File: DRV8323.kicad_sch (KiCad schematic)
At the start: 32 parts, among them J3 Screw_Terminal_01x02, U10 NTMFS5C628NLT1G, U11 NTMFS5C628NLT1G, U12 NTMFS5C628NLT1G, U13 LM393, U5 DRV8323RSRGZR, U6 NTMFS5C628NLT1G, U7 NTMFS5C628NLT1G, U8 NTMFS5C628NLT1G, U9 NTMFS5C628NLT1G

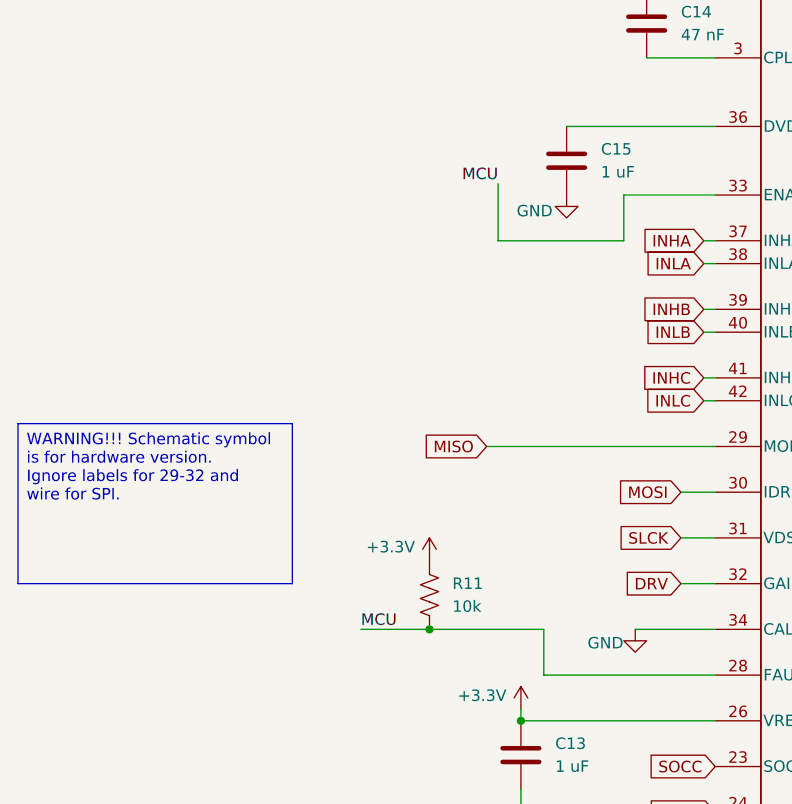
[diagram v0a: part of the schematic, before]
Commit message: Added additional Labels
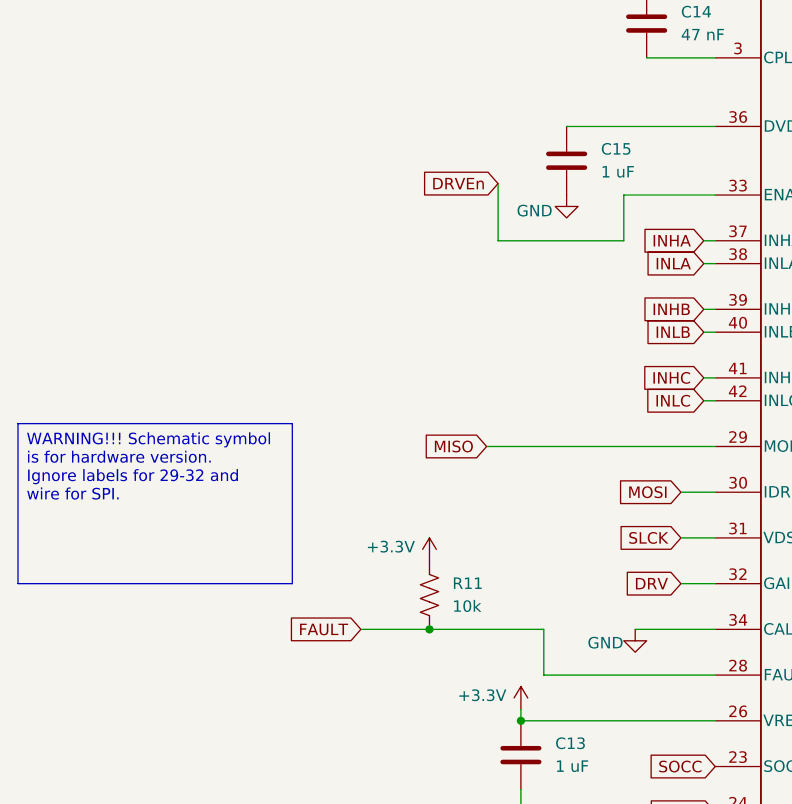
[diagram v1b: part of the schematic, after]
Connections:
- net MCU renamed FAULT
- net FAULT: no longer U5.33 (ENABLE)
- new net DRVEn: U5.33 (ENABLE)
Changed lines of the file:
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@@
-		)
-	)
-	(label "MCU"
-		(at 25.4 110.49 0)
-		(effects
-			(font
-				(size 1.27 1.27)
-			)
-			(justify left bottom)
 		)
 	)
@@
 		)
 	)
-	(label "MCU"
-		(at 40.64 60.96 180)
-		(effects
-			(font
-				(size 1.27 1.27)
-			)
-			(justify right bottom)
-		)
-	)
 	(label "CurrentSense_B"
 		(at 204.47 101.6 180)
@@
 			(effects
 				(font
+					(size 1.27 1.27)
+				)
+				(justify right)
+				(hide yes)
+			)
+		)
+	)
+	(global_label "DRVEn"
+		(shape input)
+		(at 40.64 60.96 180)
+		(fields_autoplaced yes)
+		(effects
+			(font
+				(size 1.27 1.27)
+			)
+			(justify right)
+		)
+		(property "Intersheetrefs" "${INTERSHEET_REFS}"
+			(at 31.7282 60.96 0)
+			(effects
+				(font
+					(size 1.27 1.27)
+				)
+				(justify right)
+				(hide yes)
+			)
+		)
+	)
+	(global_label "FAULT"
+		(shape input)
+		(at 25.4 110.49 180)
+		(fields_autoplaced yes)
+		(effects
+			(font
+				(size 1.27 1.27)
+			)
+			(justify right)
+		)
+		(property "Intersheetrefs" "${INTERSHEET_REFS}"
+			(at 16.9114 110.49 0)
+			(effects
+				(font

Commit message: Layed out PCB
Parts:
- removed C19, C20, C21: 470 uF, symbol Device:C
- added C1, C19, C20: 470 uF, Capacitor_SMD:CP_Elec_10x12.5, symbol Device:C_Polarized
- added J4: Screw_Terminal_01x03, TerminalBlocks:TerminalBlock_MetzConnect_Type703_RT10N03HGLU_1x03_P9.52mm_Horizontal, symbol Connector:Screw_Terminal_01x03
- C13, C15, C16: footprint (none) -> Capacitor_SMD:C_0402_1005Metric
- C14, C17: footprint (none) -> Capacitor_SMD:C_0603_1608Metric
- C18, C22, C23: footprint (none) -> Capacitor_SMD:C_0805_2012Metric
- J3: footprint (none) -> TerminalBlocks:TerminalBlock_MetzConnect_Type703_RT10N02HGLU_1x02_P9.52mm_Horizontal
- NT1: footprint (none) -> NetTie:NetTie-2_SMD_Pad0.5mm
- R11, R12, R13, R14, R15, R16, R17: footprint (none) -> Resistor_SMD:R_0603_1608Metric
- R7, R8, R9: footprint (none) -> Resistor_SMD:R_2512_6332Metric
- U13: footprint (none) -> Package_SO:SOIC-8_3.9x4.9mm_P1.27mm
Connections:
- net +24V: now also C1.1, C19.1, C20.1; no longer J3.1 (Pin_1), U7.5 (DRIAN), U7.6 (EPAD)
- net GND: now also C1.2, C19.2, C20.2
- net PhaseA: now also J4.3 (Pin_3)
- net PhaseB: now also J4.2 (Pin_2)
- net PhaseC: now also U12.1 (SOURCE), U12.2 (SOURCE), U12.3 (SOURCE), U5.19 (SHC), J4.1 (Pin_1)
- new net: J3.1 (Pin_1), U7.5 (DRIAN), U7.6 (EPAD)

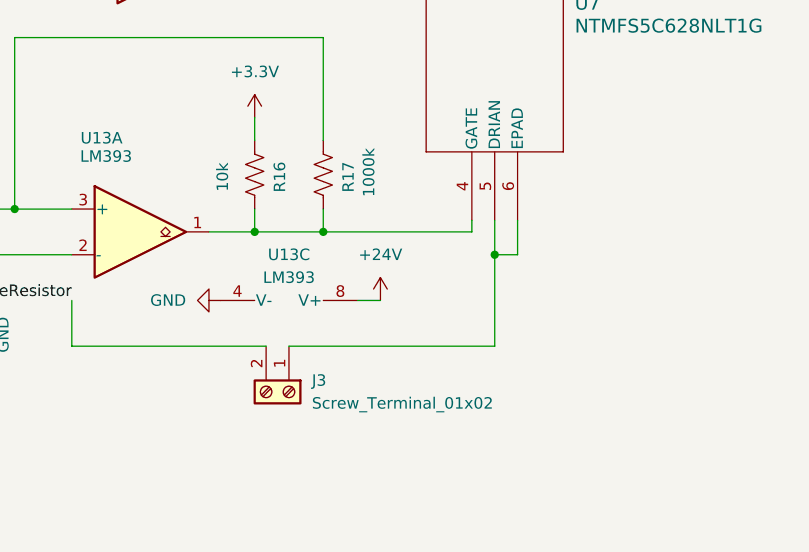
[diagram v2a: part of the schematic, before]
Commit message: finalizing PCB Layouts and traces
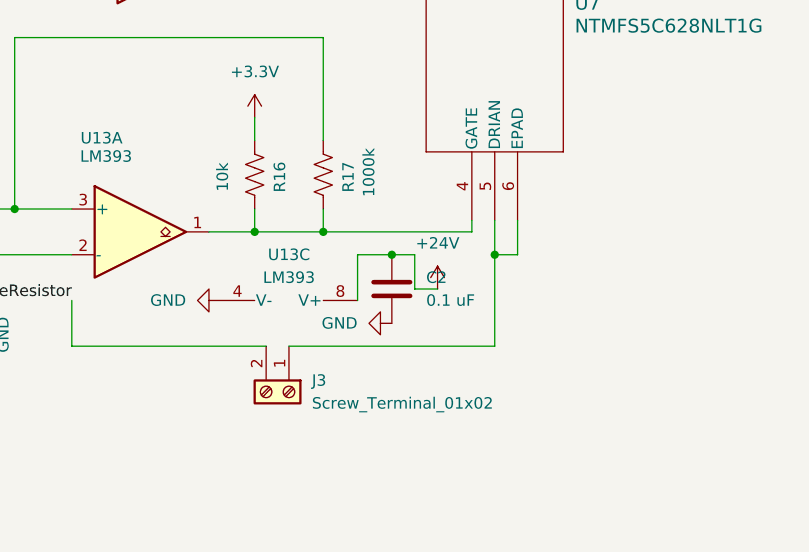
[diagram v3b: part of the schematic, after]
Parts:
- added C2: 0.1 uF, Capacitor_SMD:C_0603_1608Metric, symbol Device:C
- U10, U11, U12, U6, U7, U8, U9: footprint ESP-32-S3-MINI-1:DFN5_5X6_ONS -> ESP-32-S3-MINI-1:NTMF_FET_FIXED
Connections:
- net +24V: now also C2.2
- net GND: now also C2.1
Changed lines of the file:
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@@
 	)
 	(junction
+		(at 257.81 153.67)
+		(diameter 0)
+		(color 0 0 0 0)
+	)
+	(junction
 		(at 215.9 148.59)
 		(diameter 0)
@@
 	(wire
 		(pts
+			(xy 254 158.75) (xy 254 153.67)
+		)
+		(stroke
+			(width 0)
+			(type default)
+		)
+	)
+	(wire
+		(pts
 			(xy 64.77 62.23) (xy 54.61 62.23)
 		)
@@
 	(wire
 		(pts
+			(xy 257.81 153.67) (xy 260.35 153.67)
+		)
+		(stroke
+			(width 0)
+			(type default)
+		)
+	)
+	(wire
+		(pts
 			(xy 201.93 53.34) (xy 201.93 50.8)
 		)
@@
 	(wire
 		(pts
+			(xy 260.35 153.67) (xy 260.35 157.48)
+		)
+		(stroke
+			(width 0)
+			(type default)
+		)
+	)
+	(wire
+		(pts
 			(xy 266.7 104.14) (xy 266.7 101.6)
 		)
@@
 	(wire
 		(pts
+			(xy 260.35 157.48) (xy 262.89 157.48)
+		)
+		(stroke
+			(width 0)
+			(type default)
+		)
+	)
+	(wire
+		(pts
+			(xy 254 153.67) (xy 257.81 153.67)
+		)
+		(stroke
+			(width 0)
+			(type default)
+		)
+	)
+	(wire
+		(pts
 			(xy 48.26 54.61) (xy 64.77 54.61)
 		)
@@
 	(wire
 		(pts
-			(xy 254 158.75) (xy 256.54 158.75)
-		)
-		(stroke
-			(width 0)
-			(type default)
-		)
-	)
-	(wire
-		(pts
 			(xy 110.49 151.13) (xy 115.57 151.13)
 		)
@@
 			)
 		)
-		(property "Footprint" "ESP-32-S3-MINI-1:DFN5_5X6_ONS"
+		(property "Footprint" "ESP-32-S3-MINI-1:NTMF_FET_FIXED"
 			(at 153.67 120.65 0)
 			(effects
@@
 	(symbol
 		(lib_id "Device:C")
+		(at 257.81 157.48 180)
+		(unit 1)
+		(exclude_from_sim no)
+		(in_bom yes)
+		(on_board yes)
+		(dnp no)
+		(fields_autoplaced yes)
+		(property "Reference" "C2"
+			(at 261.62 156.2099 0)
+			(effects
+				(font
+					(size 1.27 1.27)
+				)
+				(justify right)
+			)
+		)
+		(property "Value" "0.1 uF"
+			(at 261.62 158.7499 0)
+			(effects
+				(font
+					(size 1.27 1.27)
+				)
+				(justify right)
+			)
+		)
+		(property "Footprint" "Capacitor_SMD:C_0603_1608Metric"
+			(at 256.8448 153.67 0)
+			(effects
+				(font
+					(size 1.27 1.27)
+				)
+				(hide yes)
+			)
+		)
+		(property "Datasheet" "~"
+			(at 257.81 157.48 0)
+			(effects
+				(font
+					(size 1.27 1.27)
+				)
+				(hide yes)
+			)
+		)
+		(property "Description" "Unpolarized capacitor"
+			(at 257.81 157.48 0)
+			(effects
+				(font
+					(size 1.27 1.27)
+				)
+				(hide yes)
+			)
+		)
+		(pin "2"
+		)
+		(pin "1"
+		)
+		(instances
+			(project "Motor_driver_board"
+				(path "/d384c841-cbb4-43a6-88c3-e1bf606ffd62/b93c4029-f99b-4aa0-b921-a6e9eb4bda3c"
+					(reference "C2")
+					(unit 1)
+				)
+			)
+		)
+	)
+	(symbol
+		(lib_id "Device:C")
 		(at 57.15 43.18 0)
 		(unit 1)
@@
 	(symbol
 		(lib_id "power:+24V")
-		(at 256.54 158.75 0)
+		(at 262.89 157.48 0)
 		(unit 1)
 		(exclude_from_sim no)
@@
 		(fields_autoplaced yes)
 		(property "Reference" "#PWR065"
-			(at 256.54 162.56 0)
+			(at 262.89 161.29 0)
 			(effects
 				(font
@@
 		)
 		(property "Value" "+24V"
-			(at 256.54 153.67 0)
+			(at 262.89 152.4 0)
 			(effects
 				(font
@@
 		)
 		(property "Footprint" ""
-			(at 256.54 158.75 0)
+			(at 262.89 157.48 0)
 			(effects
 				(font
@@
 		)
 		(property "Datasheet" ""
-			(at 256.54 158.75 0)
+			(at 262.89 157.48 0)
 			(effects
 				(font
@@
 		)
 		(property "Description" "Power symbol creates a global label with name \"+24V\""
-			(at 256.54 158.75 0)
+			(at 262.89 157.48 0)
 			(effects
 				(font
@@
 			)
 		)
-		(property "Footprint" "ESP-32-S3-MINI-1:DFN5_5X6_ONS"
+		(property "Footprint" "ESP-32-S3-MINI-1:NTMF_FET_FIXED"
 			(at 271.78 104.14 0)
 			(effects
@@
 			)
 		)
-		(property "Footprint" "ESP-32-S3-MINI-1:DFN5_5X6_ONS"
+		(property "Footprint" "ESP-32-S3-MINI-1:NTMF_FET_FIXED"
 			(at 233.68 67.31 0)
 			(effects
@@
 			)
 		)
-		(property "Footprint" "ESP-32-S3-MINI-1:DFN5_5X6_ONS"
+		(property "Footprint" "ESP-32-S3-MINI-1:NTMF_FET_FIXED"
 			(at 179.07 93.98 0)
 			(effects
@@
 			)
 		)
-		(property "Footprint" "ESP-32-S3-MINI-1:DFN5_5X6_ONS"
+		(property "Footprint" "ESP-32-S3-MINI-1:NTMF_FET_FIXED"
 			(at 201.93 99.06 0)
 			(effects
@@
 	(symbol
 		(lib_id "power:GND")
+		(at 257.81 161.29 270)
+		(unit 1)
+		(exclude_from_sim no)
+		(in_bom yes)
+		(on_board yes)
+		(dnp no)
+		(fields_autoplaced yes)
+		(property "Reference" "#PWR073"
+			(at 251.46 161.29 0)
+			(effects
+				(font
+					(size 1.27 1.27)
+				)
+				(hide yes)
+			)
+		)
+		(property "Value" "GND"
+			(at 254 161.2899 90)
+			(effects
+				(font
+					(size 1.27 1.27)
+				)
+				(justify right)
+			)
+		)
+		(property "Footprint" ""
+			(at 257.81 161.29 0)
+			(effects
+				(font
+					(size 1.27 1.27)
+				)
+				(hide yes)
+			)
+		)
+		(property "Datasheet" ""
+			(at 257.81 161.29 0)
+			(effects
+				(font
+					(size 1.27 1.27)
+				)
+				(hide yes)
+			)
+		)
+		(property "Description" "Power symbol creates a global label with name \"GND\" , ground"
+			(at 257.81 161.29 0)
+			(effects
+				(font
+					(size 1.27 1.27)
+				)
+				(hide yes)
+			)
+		)
+		(pin "1"
+		)
+		(instances
+			(project "Motor_driver_board"
+				(path "/d384c841-cbb4-43a6-88c3-e1bf606ffd62/b93c4029-f99b-4aa0-b921-a6e9eb4bda3c"
+					(reference "#PWR073")
+					(unit 1)
+				)
+			)
+		)
+	)
+	(symbol
+		(lib_id "power:GND")
 		(at 48.26 62.23 0)
 		(unit 1)
@@
 			)
 		)
-		(property "Footprint" "ESP-32-S3-MINI-1:DFN5_5X6_ONS"
+		(property "Footprint" "ESP-32-S3-MINI-1:NTMF_FET_FIXED"
 			(at 134.62 114.3 0)
 			(effects
@@
 			)
 		)
-		(property "Footprint" "ESP-32-S3-MINI-1:DFN5_5X6_ONS"
+		(property "Footprint" "ESP-32-S3-MINI-1:NTMF_FET_FIXED"
 			(at 264.16 74.93 0)
 			(effects

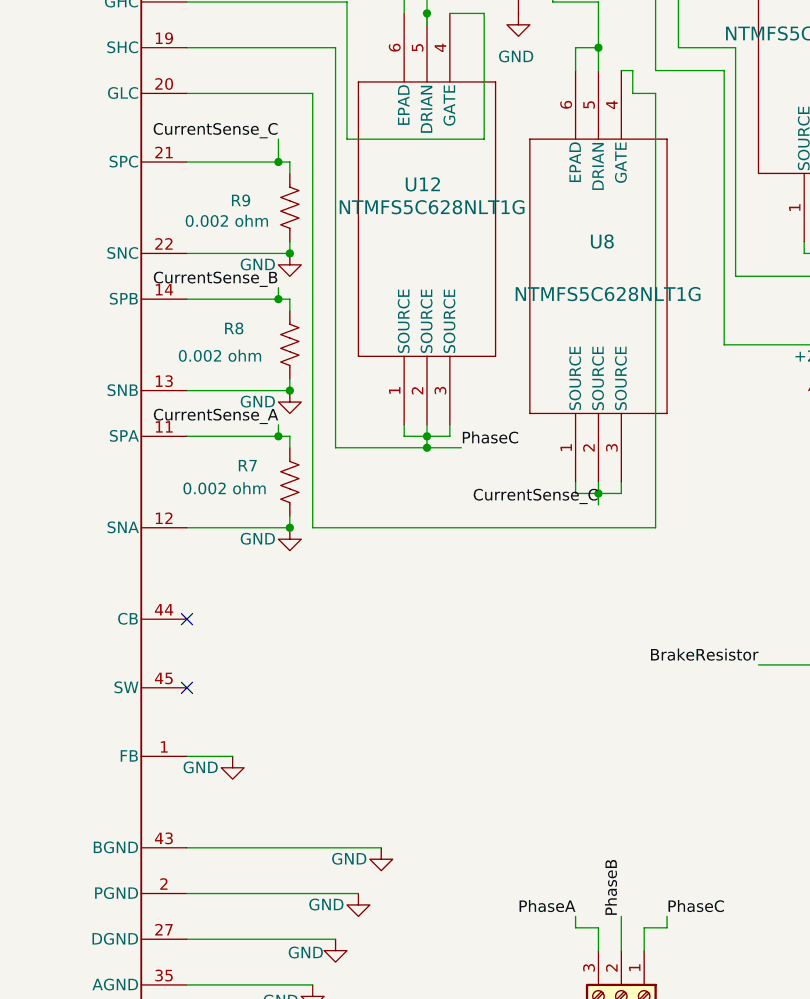
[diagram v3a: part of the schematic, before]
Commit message: removed unnecessary regulators and replaced with cheaper buck
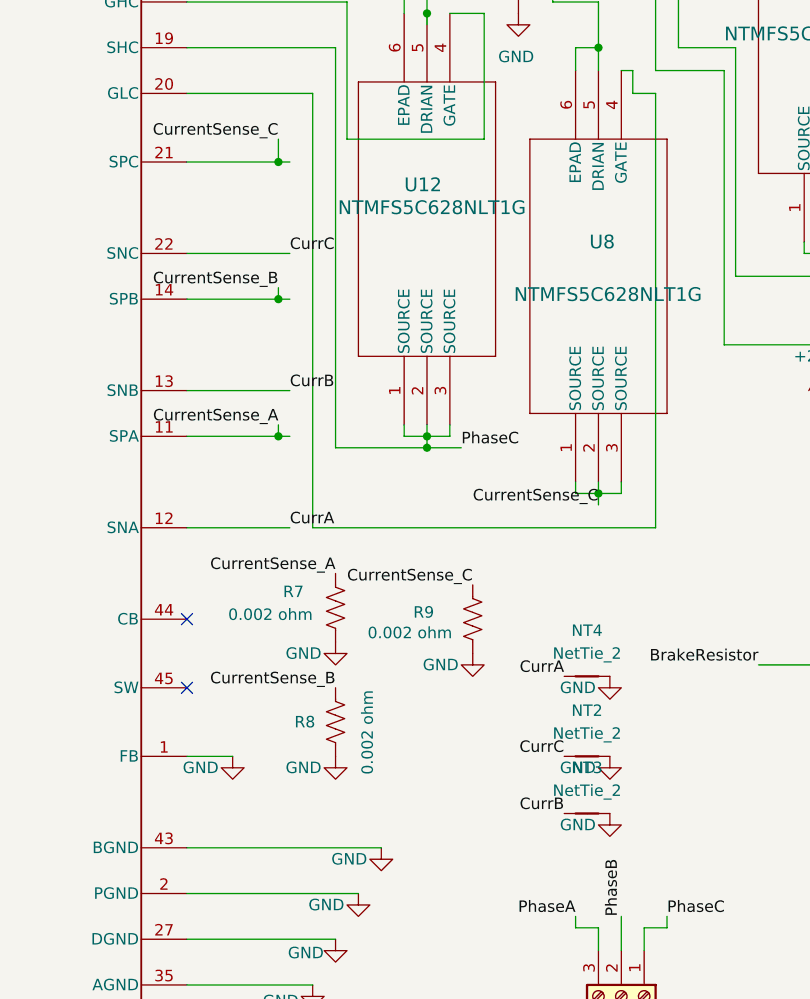
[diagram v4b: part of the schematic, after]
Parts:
- added NT2, NT3, NT4: NetTie_2, NetTie:NetTie-2_SMD_Pad0.5mm, symbol Device:NetTie_2
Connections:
- net GND: now also NT2.2, NT3.2, NT4.2; no longer U5.12 (SNA), U5.13 (SNB), U5.22 (SNC)
- new net CurrA: NT4.1, U5.12 (SNA)
- new net CurrB: NT3.1, U5.13 (SNB)
- new net CurrC: NT2.1, U5.22 (SNC)
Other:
- moved on the sheet: R7, R8, R9

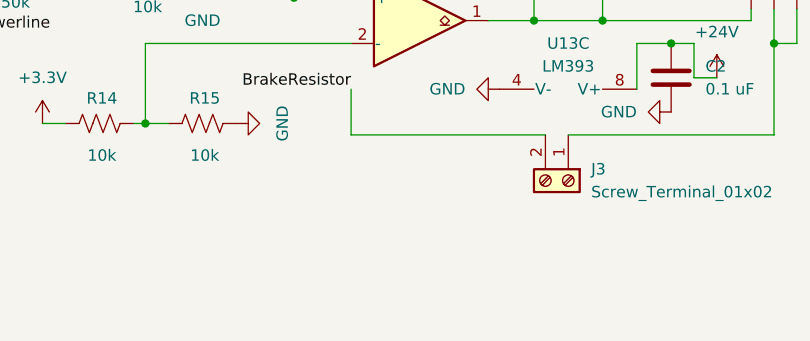
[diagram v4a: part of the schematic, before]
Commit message: changed regulators, added resistor for slew rate on braking mosfet
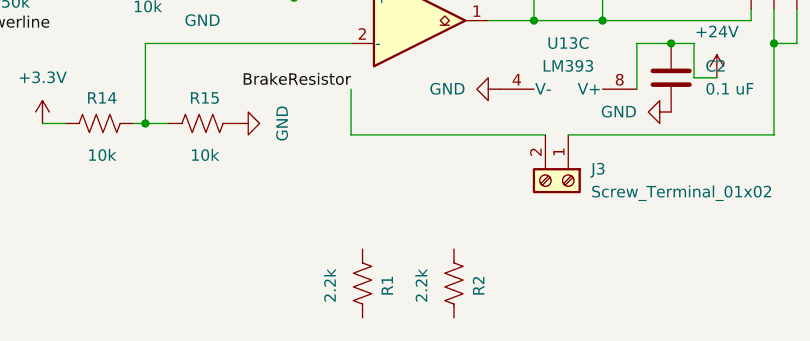
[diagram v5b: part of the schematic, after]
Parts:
- added R1, R2: 2.2k, Resistor_SMD:R_0603_1608Metric, symbol Device:R_US
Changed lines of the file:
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@@
+	(symbol
+		(lib_id "Device:R_US")
+		(at 233.68 180.34 180)
+		(unit 1)
+		(exclude_from_sim no)
+		(in_bom yes)
+		(on_board yes)
+		(dnp no)
+		(property "Reference" "R2"
+			(at 236.474 180.594 90)
+			(effects
+				(font
+					(size 1.27 1.27)
+				)
+			)
+		)
+		(property "Value" "2.2k"
+			(at 230.124 180.594 90)
+			(effects
+				(font
+					(size 1.27 1.27)
+				)
+			)
+		)
+		(property "Footprint" "Resistor_SMD:R_0603_1608Metric"
+			(at 232.664 180.086 90)
+			(effects
+				(font
+					(size 1.27 1.27)
+				)
+				(hide yes)
+			)
+		)
+		(property "Datasheet" "~"
+			(at 233.68 180.34 0)
+			(effects
+				(font
+					(size 1.27 1.27)
+				)
+				(hide yes)
+			)
+		)
+		(property "Description" "Resistor, US symbol"
+			(at 233.68 180.34 0)
+			(effects
+				(font
+					(size 1.27 1.27)
+				)
+				(hide yes)
+			)
+		)
+		(pin "2"
+		)
+		(pin "1"
+		)
+		(instances
+			(project "Motor_driver_board"
+				(path "/d384c841-cbb4-43a6-88c3-e1bf606ffd62/b93c4029-f99b-4aa0-b921-a6e9eb4bda3c"
+					(reference "R2")
+					(unit 1)
+				)
+			)
+		)
+	)
 	(symbol
 		(lib_id "Device:R_US")
@@
 					(unit 1)
 				)
+			)
+		)
+	)
+	(symbol
+		(lib_id "Device:R_US")
+		(at 223.52 180.34 180)
+		(unit 1)
+		(exclude_from_sim no)
+		(in_bom yes)
+		(on_board yes)
+		(dnp no)
+		(property "Reference" "R1"
+			(at 226.314 180.594 90)
+			(effects
+				(font
+					(size 1.27 1.27)
+				)
+			)
+		)
+		(property "Value" "2.2k"
+			(at 219.964 180.594 90)
+			(effects
+				(font
+					(size 1.27 1.27)
+				)
+			)
+		)
+		(property "Footprint" "Resistor_SMD:R_0603_1608Metric"
+			(at 222.504 180.086 90)
+			(effects
+				(font
+					(size 1.27 1.27)
+				)
+				(hide yes)
+			)
+		)
+		(property "Datasheet" "~"
+			(at 223.52 180.34 0)
+			(effects
+				(font
+					(size 1.27 1.27)
+				)
+				(hide yes)
+			)
+		)
+		(property "Description" "Resistor, US symbol"
+			(at 223.52 180.34 0)
+			(effects
+				(font
+					(size 1.27 1.27)
+				)
+				(hide yes)
+			)
+		)
+		(pin "2"
+		)
+		(pin "1"
+		)
+		(instances
+			(project "Motor_driver_board"
+				(path "/d384c841-cbb4-43a6-88c3-e1bf606ffd62/b93c4029-f99b-4aa0-b921-a6e9eb4bda3c"
+					(reference "R1")
+					(unit 1)
+				)
